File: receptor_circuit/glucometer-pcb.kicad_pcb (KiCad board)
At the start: 2 copper layers, 36.9 x 68.2 mm, 21 parts

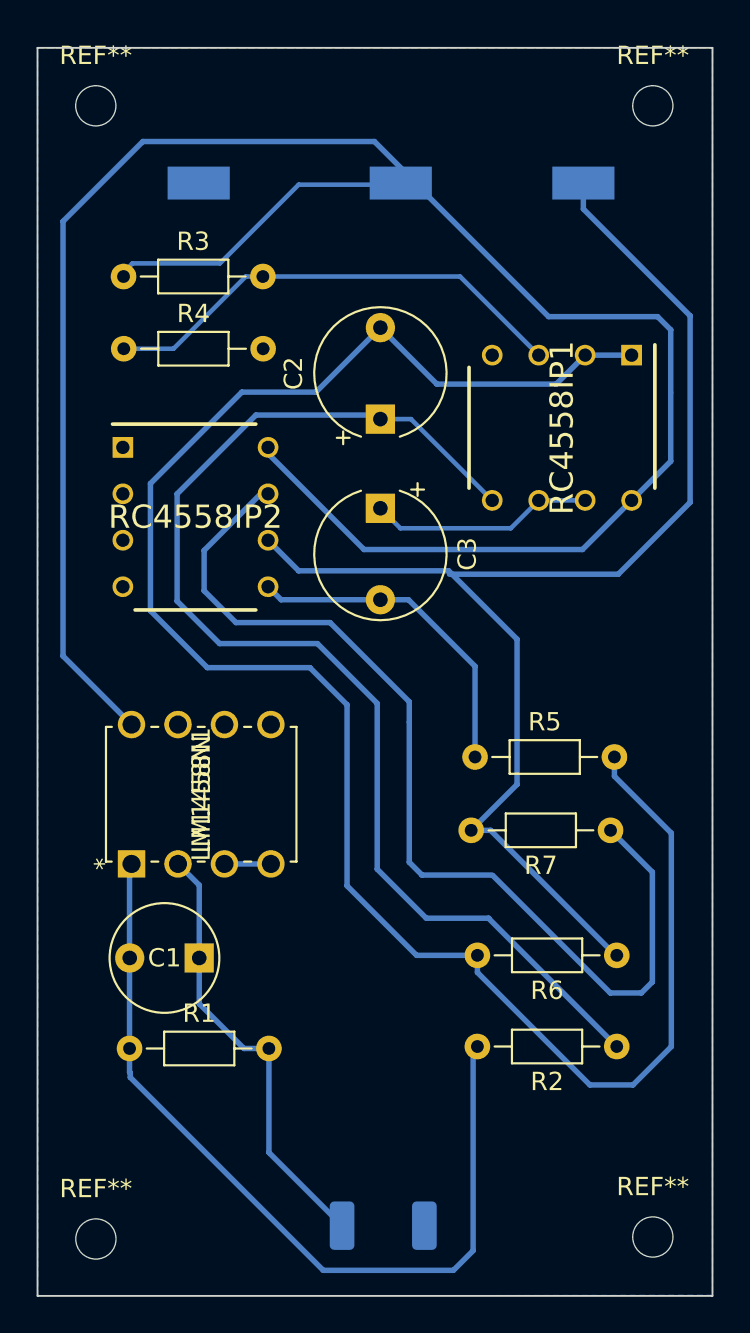
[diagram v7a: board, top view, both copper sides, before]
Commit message: receptor footprint update
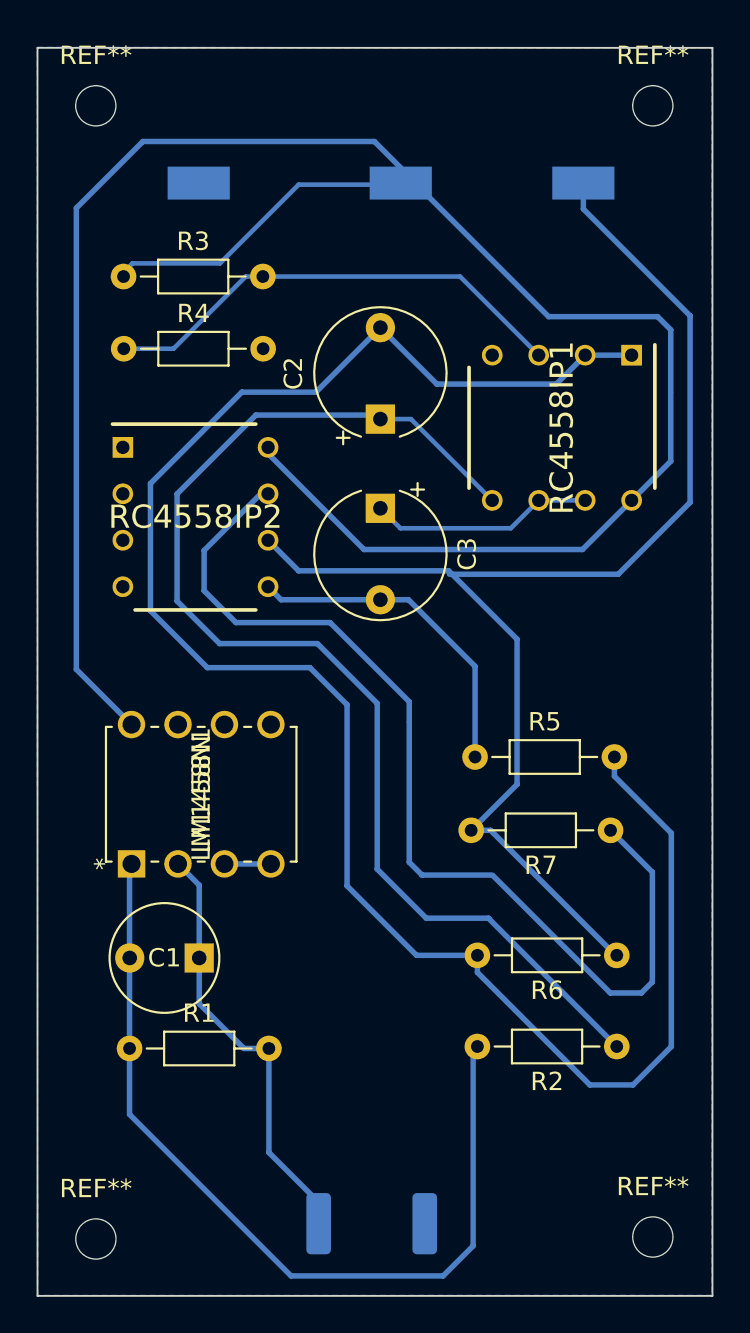
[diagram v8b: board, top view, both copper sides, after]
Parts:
- RECEPTOR_DIODE1: footprint LED_SMD:LED_2010_5025Metric -> LED_SMD:LED_2512_6332Metric
- moved RECEPTOR_DIODE1 0.64 mm to (190.9, 172.2)
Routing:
- net Net-(C1-Pad2): track 46.9 -> 48.2 mm
- net Net-(C1-Pad1): track 24.3 -> 23.7 mm
- net VCC: track 119.9 -> 119.3 mm
